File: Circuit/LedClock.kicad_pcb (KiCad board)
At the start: 2 copper layers, 21 parts, among them U1 MSP430G2553IPW20

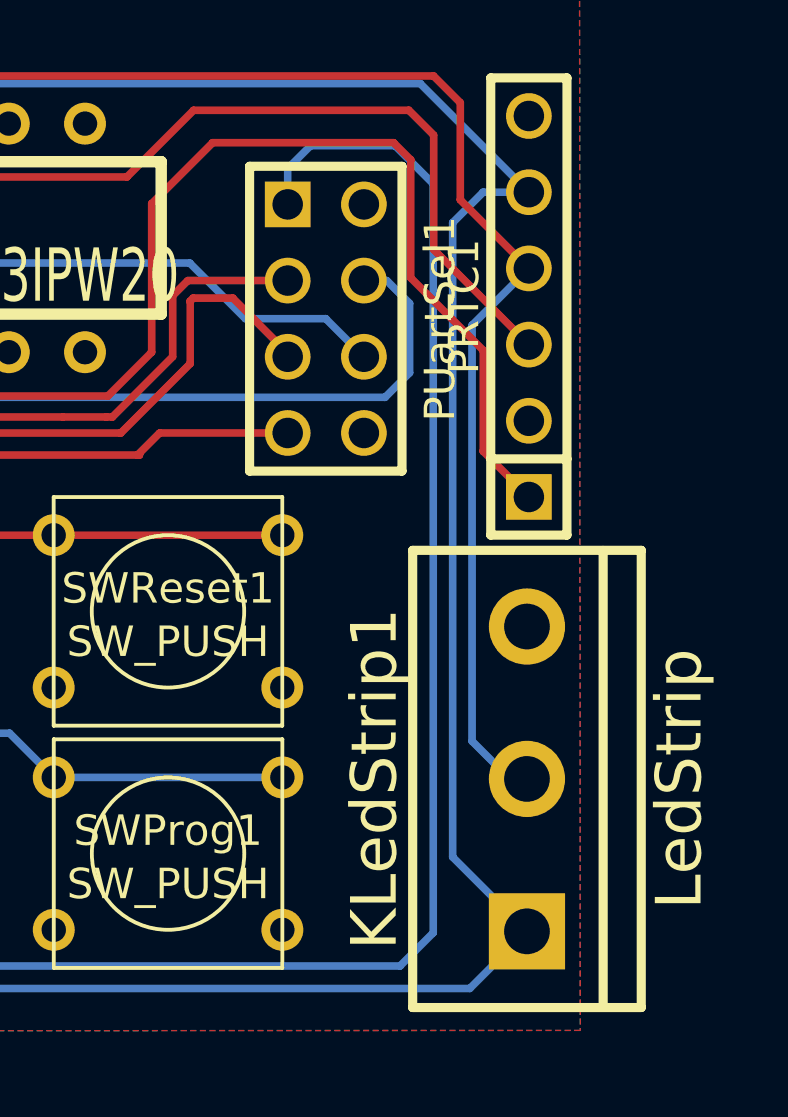
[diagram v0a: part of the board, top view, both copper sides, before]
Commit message: Added current limiting resistor on the ledstrip data line Adviced by adafruit
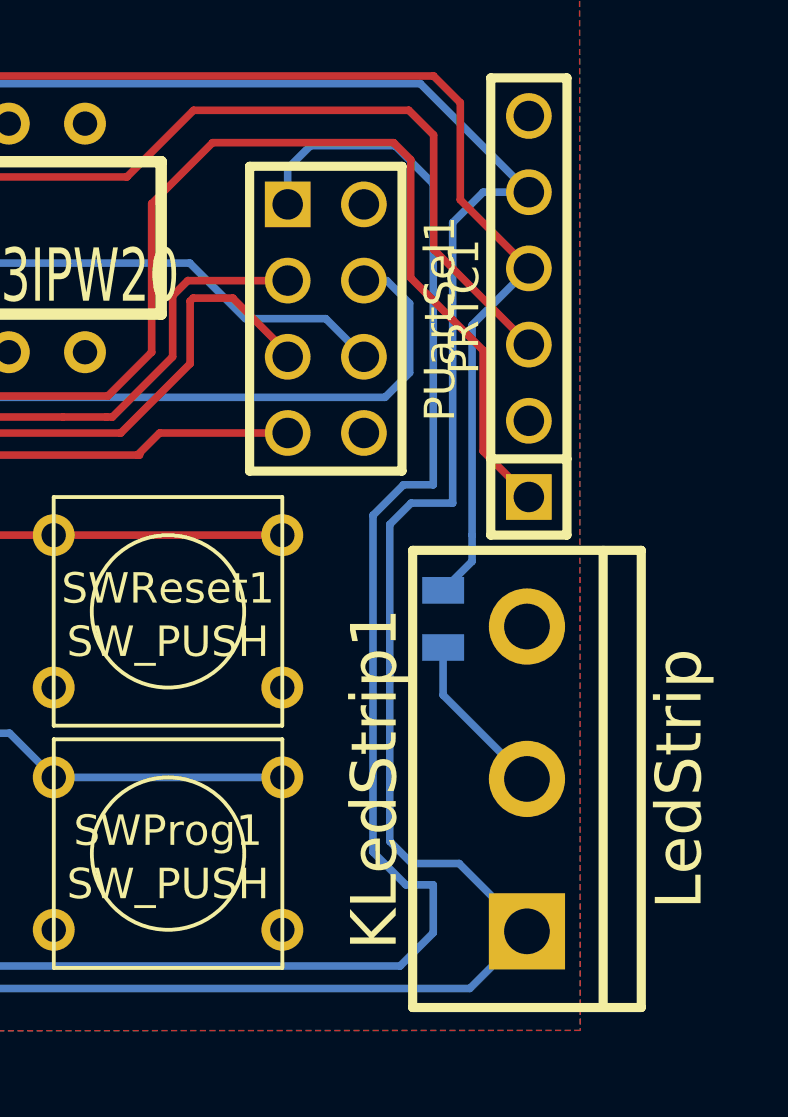
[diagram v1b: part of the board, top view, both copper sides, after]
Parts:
- added R4: 220, SM0805, B.Cu at (55.0, 34.7)
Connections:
- KLedStrip1 pad 2: N-0000020 (its old number) -> N-000002
- PRTC1 pad 4: N-0000020 (its old number) -> N-0000015
- R1 pad 1: N-0000020 (its old number) -> N-0000015
- U1 pad 15: N-0000020 (its old number) -> N-0000015
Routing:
- net N-0000020 (its old number): track 66.8 -> 0.00 mm
- net N-0000015: track 0.00 -> 59.8 mm
- net N-000002: track 0.00 -> 5.54 mm
- net +5V: track 129.2 -> 132.7 mm
- net N-0000020: track 62.1 -> 64.9 mm

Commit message: Updated layout to fit the new ring and stay within 10*5cm
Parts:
- added K1: PROG, SIL-3, F.Cu at (204.1, 231.1)
- added SW1: MSP_RESET, SW_PUSH_SMALL, F.Cu at (204.3, 240.2)
- R3: moved to F.Cu
- moved R1 301.4 mm to (224.0, 232.5), turned to 0 degrees
- moved R2 296.8 mm to (219.7, 232.5), turned to 180 degrees
- moved UartToSerial1 296.7 mm to (270.2, 204.4)
- moved USB_SERIAL1 294.0 mm to (257.4, 202.3), turned to 270 degrees
- moved R46k1 292.3 mm to (267.3, 211.3), turned to 270 degrees
- moved R10k1 290.0 mm to (211.6, 233.1), turned to 180 degrees
- moved RLDR1 289.3 mm to (231.2, 218.7), turned to 180 degrees
- moved R3 288.2 mm to (226.5, 219.0), turned to 180 degrees
- moved R46K2 288.0 mm to (265.0, 211.4), turned to 270 degrees
- moved Uref1 287.7 mm to (232.9, 234.1), turned to 270 degrees
- moved KPIR1 280.4 mm to (204.1, 228.0), turned to 0 degrees
- moved U1 278.8 mm to (222.5, 225.3), turned to 180 degrees
- moved C100uF1 278.4 mm to (223.3, 239.0), turned to 180 degrees
- moved SWReset1 276.6 mm to (248.4, 222.8)
- moved PUartSel1 275.5 mm to (240.3, 225.0)
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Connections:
- ESP1 pad 10: GND -> (no net)
- ESP1 pad 12: (no net) -> GND
- ESP1 pad 13: (no net) -> N-0000027
- ESP1 pad 14: +3.3V -> N-0000027
- ESP1 pad 8: N-0000018 -> +3.3V
- ESP1 pad 9: N-0000018 -> (no net)
- R46K2 pad 2: N-0000018 -> N-0000027
- SWProg1 pad 1: N-0000018 -> N-0000027
- U1 pad 17: (no net) -> N-0000023
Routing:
- net N-0000024: track 59.8 -> 102.9 mm
- net N-0000027: track 0.00 -> 39.8 mm
- net N-0000018: track 33.1 -> 0.00 mm
- net N-0000023: track 0.00 -> 28.5 mm
- net N-0000013: track 15.3 -> 42.9 mm
- net N-000002: track 23.8 -> 48.6 mm
- net N-0000025: track 50.9 -> 73.1 mm
- net N-000007: track 31.7 -> 11.2 mm
- net N-000006: track 64.9 -> 45.8 mm, vias 1 -> 0
- net N-0000020: track 33.1 -> 19.5 mm
- net N-000001: track 27.8 -> 15.0 mm
- net N-0000021: track 34.6 -> 22.9 mm
- net +5V: track 132.7 -> 121.2 mm, vias 1 -> 2
- net N-000008: track 13.9 -> 23.2 mm, vias 1 -> 0
- net N-0000010: track 43.7 -> 52.5 mm
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
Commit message: Updated pcb w.r.t design rules and unconnected parts
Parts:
- moved R46K2 219.8 mm to (122.2, 44.2)
- moved R10k1 219.8 mm to (68.9, 66.0)
- moved C100uF1 219.8 mm to (80.6, 71.8)
- moved C100uF2 219.8 mm to (80.5, 68.7)
- moved ESP1 219.8 mm to (103.0, 44.2)
- moved K1 219.8 mm to (61.4, 64.0)
- moved KLedStrip1 219.8 mm to (52.7, 70.1)
- moved KPIR1 219.8 mm to (61.3, 60.9)
- moved PPower1 219.8 mm to (71.3, 71.8)
- moved PRTC1 219.8 mm to (126.8, 30.0)
- moved PUartSel1 219.8 mm to (97.5, 57.9)
- moved R1 219.8 mm to (81.2, 65.4)
- moved R2 219.8 mm to (77.0, 65.4)
- moved R3 219.8 mm to (83.8, 51.9)
- moved R4 219.8 mm to (61.6, 67.0)
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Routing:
- net GND: track 36.6 -> 49.5 mm, vias 3 -> 4
- net N-0000027: track 39.8 -> 47.4 mm
- net N-0000010: track 52.5 -> 57.5 mm
- net (no net): track 2.58 -> 0.07 mm, vias 2 -> 1
- net +5V: track 121.2 -> 122.0 mm

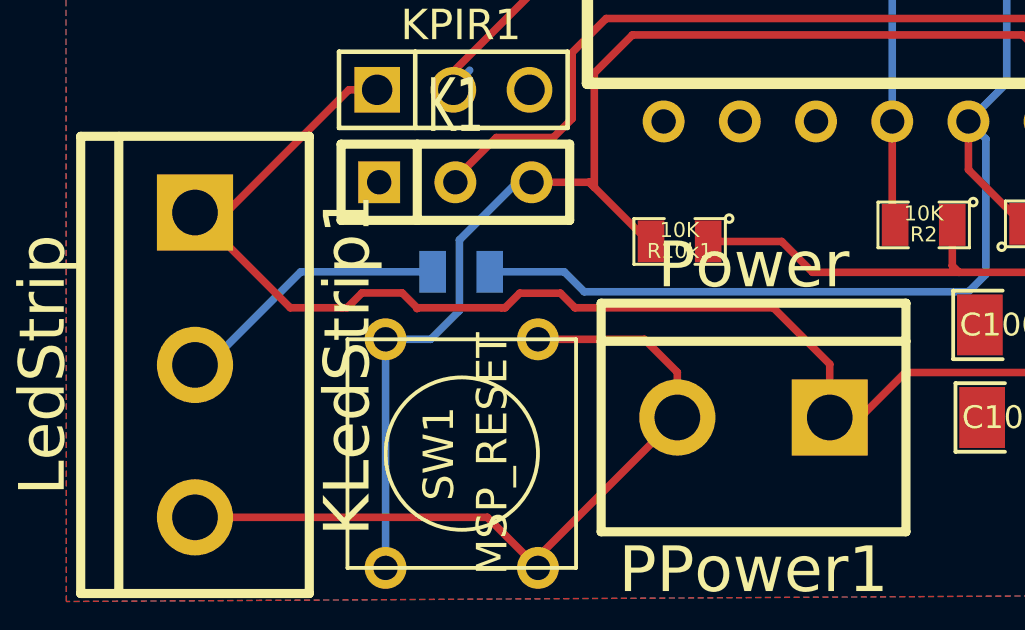
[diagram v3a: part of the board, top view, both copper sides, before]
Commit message: Updated width of power line accoording to spec
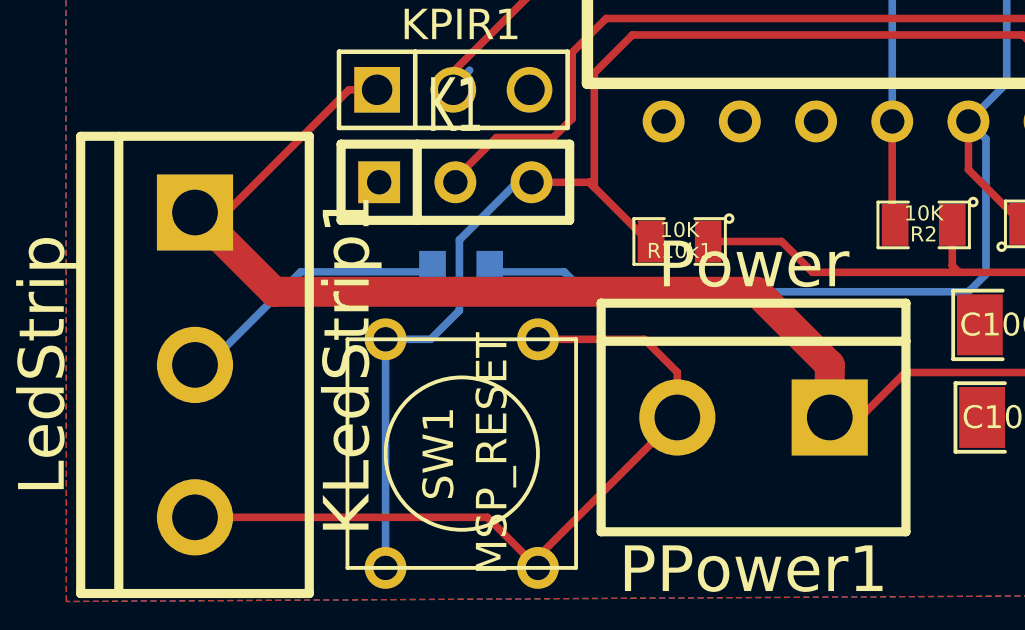
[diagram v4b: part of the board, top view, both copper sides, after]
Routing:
- net +5V: track 122.0 -> 121.2 mm
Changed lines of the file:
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@@
   (general
     (links 69)
-    (no_connects 0)
+    (no_connects 1)
     (area 17.070399 -81.888001 187.552001 93.419601)
     (thickness 1.6)
     (drawings 2)
-    (tracks 306)
+    (tracks 294)
     (zones 0)
     (modules 24)
@@
   (layers
     (15 F.Cu signal)
-    (0 B.Cu signal)
+    (0 B.Cu signal hide)
     (16 B.Adhes user)
     (17 F.Adhes user)
@@
   )
   (setup
-    (last_trace_width 0.254)
+    (last_trace_width 1)
+    (user_trace_width 0.508)
+    (user_trace_width 1)
     (trace_clearance 0.254)
     (zone_clearance 0.508)
@@
   (via (at 117.2083 43.7515) (size 0.889) (layers F.Cu B.Cu) (net 1))
   (segment (start 118.8466 42.7228) (end 119.3927 43.2689) (width 0.254) (layer B.Cu) (net 1))
-  (segment (start 62.92342 68.1736) (end 63.0428 68.1736) (width 0.254) (layer F.Cu) (net 2))
-  (segment (start 64.88684 67.68846) (end 65.37198 68.1736) (width 0.254) (layer F.Cu) (net 2))
-  (segment (start 63.52794 67.68846) (end 64.88684 67.68846) (width 0.254) (layer F.Cu) (net 2))
-  (segment (start 63.0428 68.1736) (end 63.52794 67.68846) (width 0.254) (layer F.Cu) (net 2))
-  (segment (start 57.59704 68.1736) (end 57.77484 68.1736) (width 0.254) (layer F.Cu) (net 2))
-  (segment (start 60.10402 68.199) (end 60.12942 68.1736) (width 0.254) (layer F.Cu) (net 2))
-  (segment (start 60.10402 68.1736) (end 60.10402 68.199) (width 0.254) (layer F.Cu) (net 2))
-  (segment (start 59.60872 67.6783) (end 60.10402 68.1736) (width 0.254) (layer F.Cu) (net 2))
-  (segment (start 58.27014 67.6783) (end 59.60872 67.6783) (width 0.254) (layer F.Cu) (net 2))
-  (segment (start 57.77484 68.1736) (end 58.27014 67.6783) (width 0.254) (layer F.Cu) (net 2))
+  (segment (start 73.8632 71.8312) (end 73.8632 70.0786) (width 1) (layer F.Cu) (net 2))
+  (segment (start 55.3466 67.6402) (end 52.705 64.9986) (width 1) (layer F.Cu) (net 2))
+  (segment (start 71.4248 67.6402) (end 55.3466 67.6402) (width 1) (layer F.Cu) (net 2))
+  (segment (start 73.8632 70.0786) (end 71.4248 67.6402) (width 1) (layer F.Cu) (net 2))
   (segment (start 52.705 64.9986) (end 53.7464 64.9986) (width 0.254) (layer F.Cu) (net 2))
   (segment (start 57.8358 60.9092) (end 58.7756 60.9092) (width 0.254) (layer F.Cu) (net 2))
@@
   (segment (start 120.7008 37.69868) (end 120.7008 45.108056) (width 0.254) (layer F.Cu) (net 2))
   (segment (start 122.10288 36.2966) (end 120.7008 37.69868) (width 0.254) (layer F.Cu) (net 2))
-  (segment (start 73.8632 71.8312) (end 73.8632 70.0532) (width 0.254) (layer F.Cu) (net 2))
-  (segment (start 71.9836 68.1736) (end 65.37198 68.1736) (width 0.254) (layer F.Cu) (net 2))
-  (segment (start 73.8632 70.0532) (end 71.9836 68.1736) (width 0.254) (layer F.Cu) (net 2))
-  (segment (start 62.92342 68.1736) (end 60.12942 68.1736) (width 0.254) (layer F.Cu) (net 2))
-  (segment (start 55.88 68.1736) (end 52.705 64.9986) (width 0.254) (layer F.Cu) (net 2))
-  (segment (start 57.59704 68.1736) (end 55.88 68.1736) (width 0.254) (layer F.Cu) (net 2))
   (segment (start 123.9393 36.2966) (end 126.2634 36.2966) (width 0.254) (layer F.Cu) (net 2))
   (segment (start 129.3114 31.2547) (end 130.6068 29.9593) (width 0.254) (layer F.Cu) (net 2))

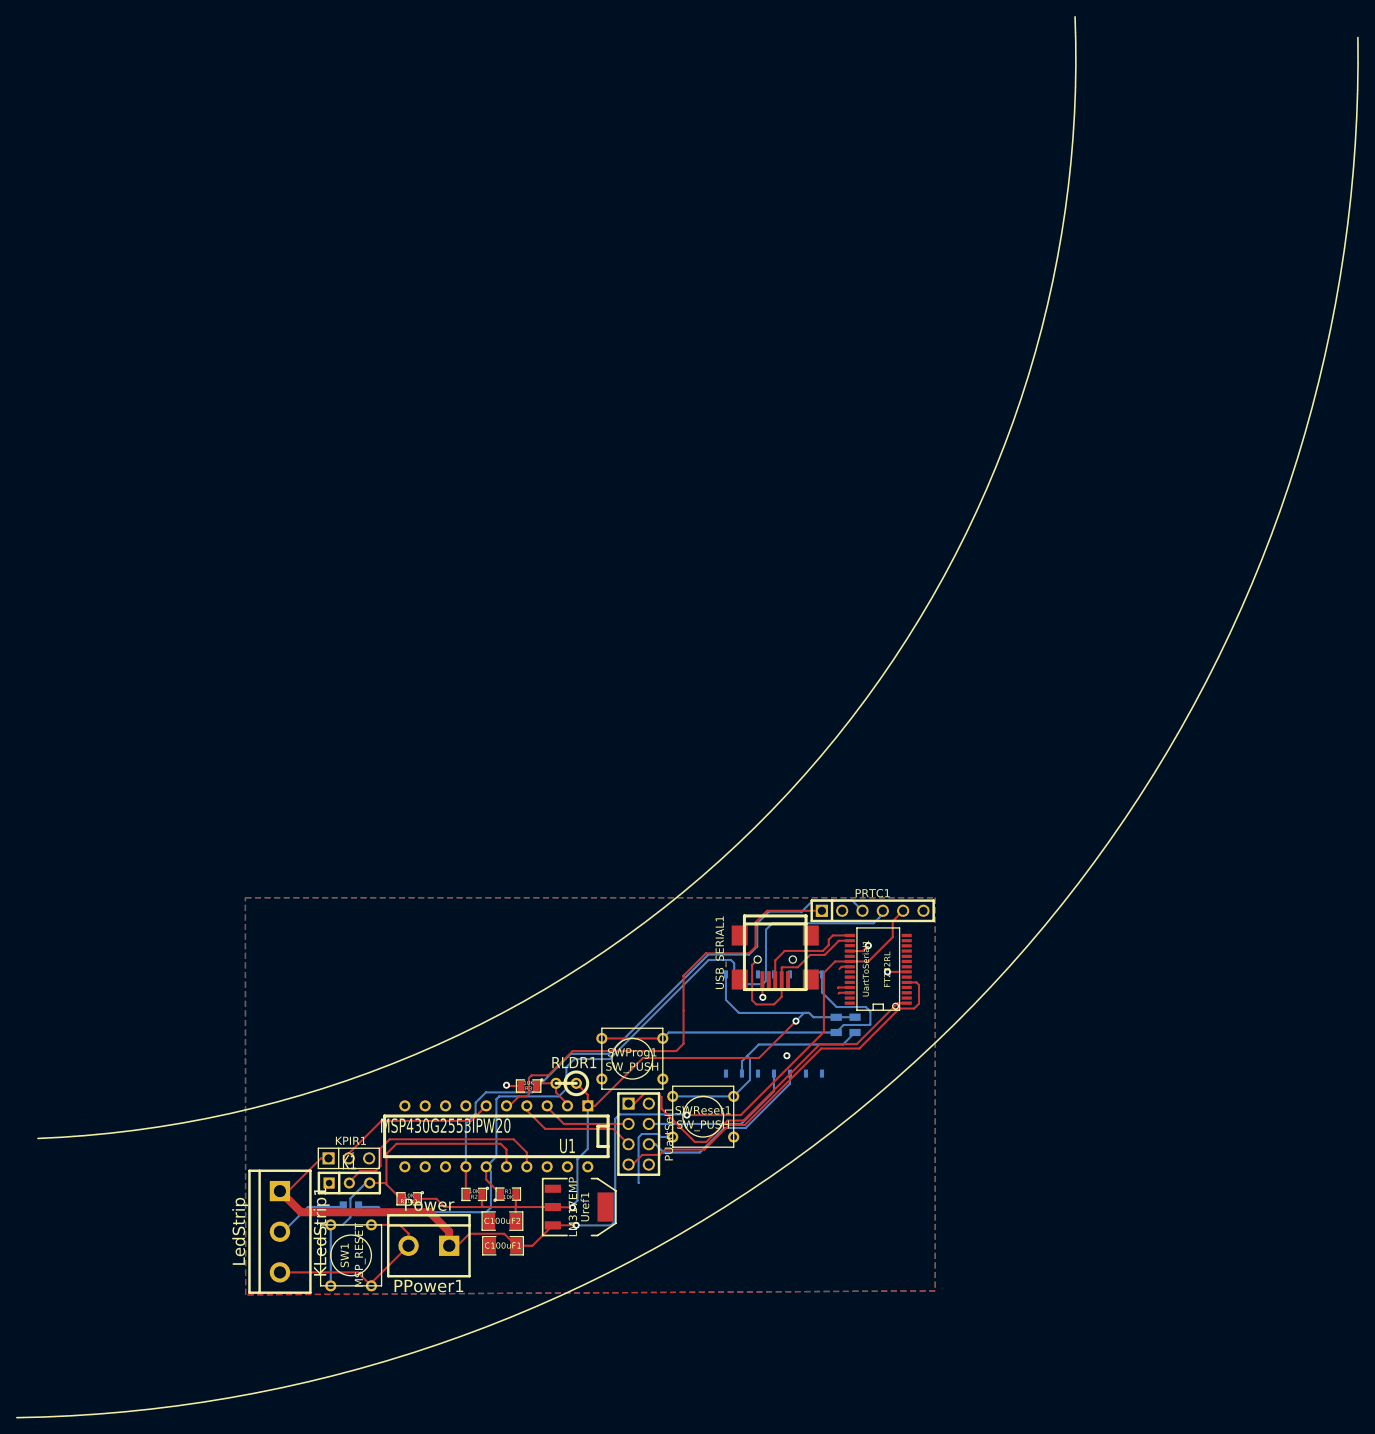
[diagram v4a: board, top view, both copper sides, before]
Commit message: Updated pcb with cutting edges, fixed minor issue and put name and version on pcb
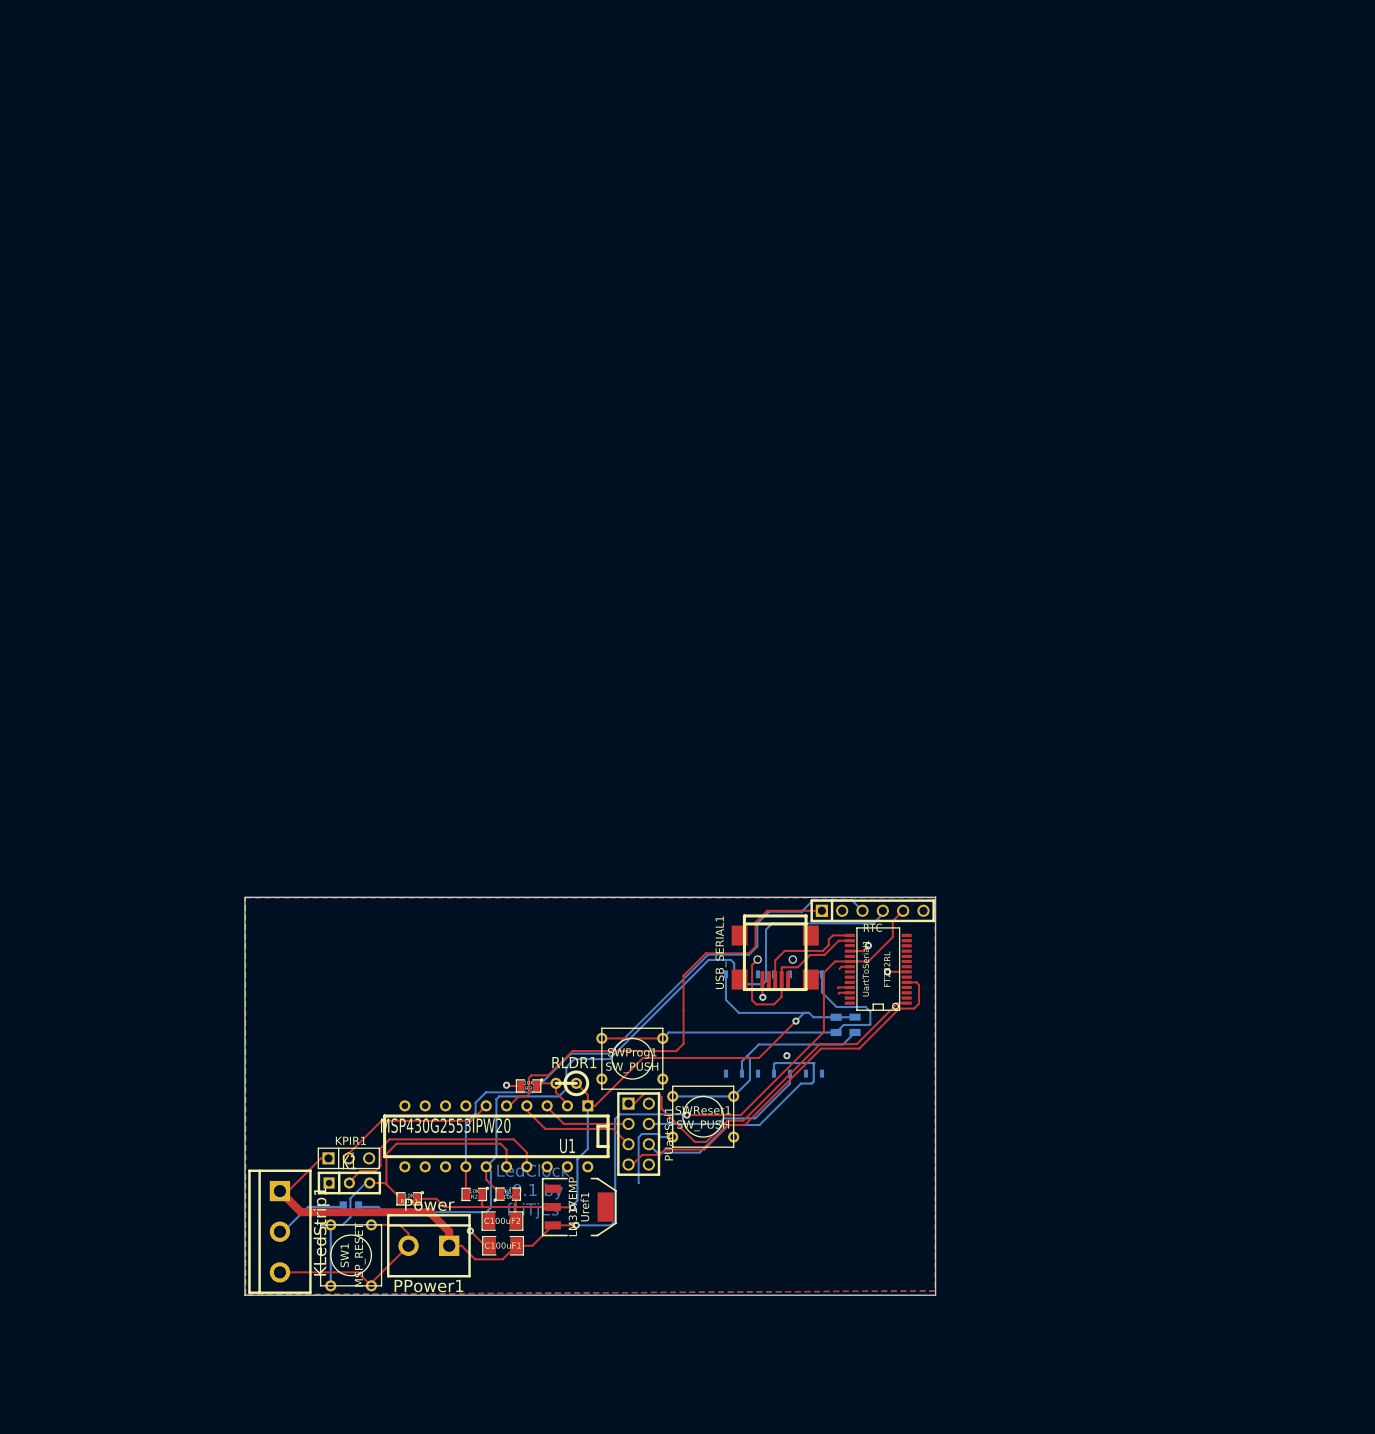
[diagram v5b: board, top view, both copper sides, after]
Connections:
- ESP1 pad 3: N-0000021 -> N-0000023
- ESP1 pad 4: N-0000020 (its old number) -> N-0000022
- PUartSel1 pad 4: N-0000020 (its old number) -> N-0000023
- PUartSel1 pad 6: N-0000021 -> N-0000022
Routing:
- net N-0000022: track 0.00 -> 33.4 mm
- net N-0000021: track 22.9 -> 0.00 mm
- net N-0000023: track 0.00 -> 21.0 mm
- net N-0000020 (its old number): track 19.5 -> 0.00 mm
- net GND: track 49.5 -> 52.7 mm, vias 4 -> 5
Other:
- board outline added: 86.3 x 49.7 mm
- board text added: "LedClock v0.1 by fLiTjEs"
